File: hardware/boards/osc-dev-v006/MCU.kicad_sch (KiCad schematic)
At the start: 17 parts, among them J2 LINKE, J3 Qwiic, U2 CH32V006F8P6

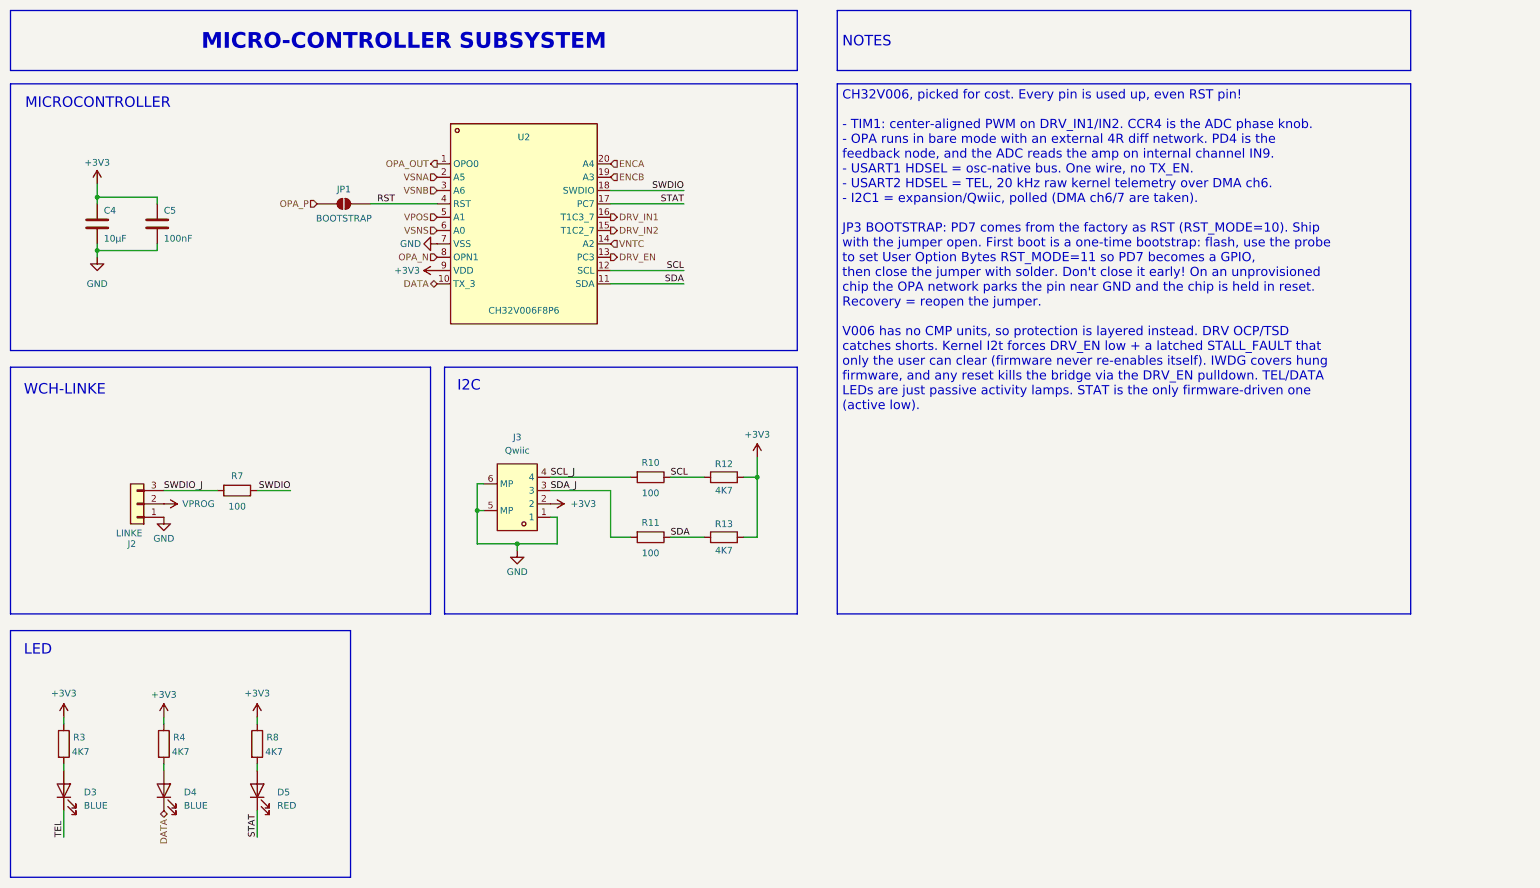
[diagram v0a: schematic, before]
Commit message: board: v006 rev-2a schematic refresh, family designators, terminal bias, tier-2 position input
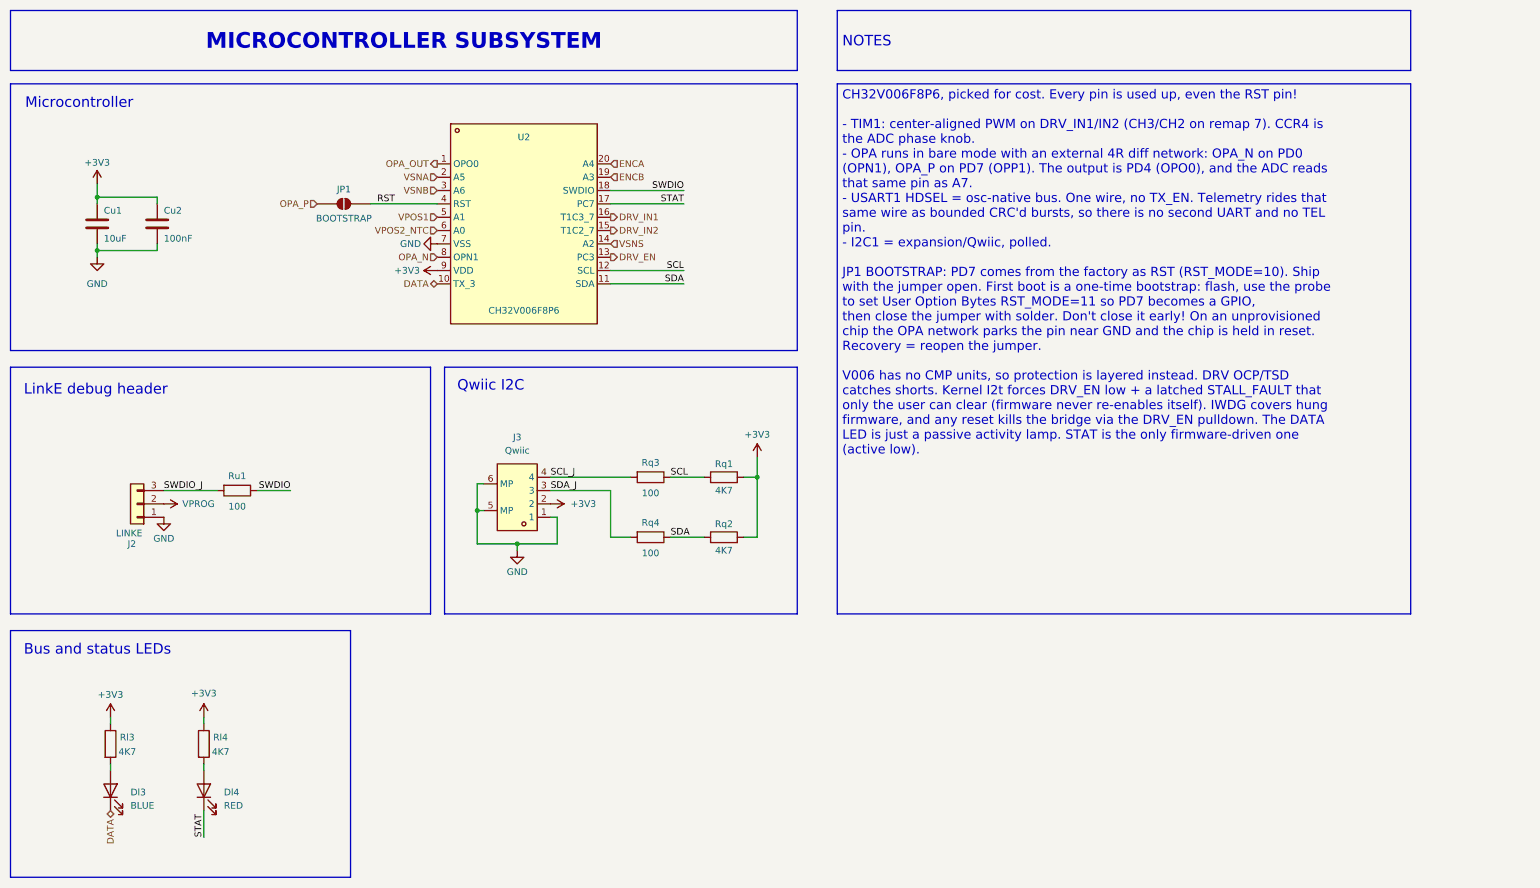
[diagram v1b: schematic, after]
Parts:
- removed D3: BLUE, LED_SMD:LED_0603_1608Metric_Pad1.05x0.95mm_HandSolder, symbol Device:LED
- removed R3: 4K7, Resistor_SMD:R_0603_1608Metric_Pad0.98x0.95mm_HandSolder, symbol Device:R
- Cu1: renamed from C4; value 10µF -> 10uF
- Dl3: renamed from D4; MFPN KT-0805B -> GL0603UB01
- Dl4: renamed from D5; LCSC C51933292 -> C497918; MFPN KT-0805R -> HL-PT-1608S52FC
- J2: footprint Connector_PinHeader_2.54mm:PinHeader_2x03_P2.54mm_Vertical -> Connector_PinHeader_2.54mm:PinHeader_1x03_P2.54mm_Vertical
- Rl3: renamed from R4; MFPN FRC0805F4701TS -> FRC0603F4701TS
- Rl4: renamed from R8; MFPN FRC0805F4701TS -> FRC0603F4701TS
- Rq1: renamed from R12; MFPN FRC0805F4701TS -> FRC0603F4701TS
- Rq2: renamed from R13; MFPN FRC0805F4701TS -> FRC0603F4701TS
- Rq3: renamed from R10; LCSC C2906981 -> C125923; MFPN FRC0805F1000TS -> (none)
- Rq4: renamed from R11; LCSC C2906981 -> C125923; MFPN FRC0805F1000TS -> (none)
- Ru1: renamed from R7; LCSC C2906981 -> C125923; MFPN FRC0805F1000TS -> (none)
- U2: JLC Type Extended -> (none)
- renumbered C5 to Cu2
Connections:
- net VNTC is gone; now on net VSNS: U2.14 (PC4)
- net VSNS: no longer U2.6 (PA2)
- net VPOS renamed VPOS1
- new net VPOS2_NTC: U2.6 (PA2)
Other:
- note added: "Bus and status LEDs"
- note added: "LinkE debug header"
- note added: "Microcontroller"
- note added: "Qwiic I2C"
- note removed: "I2C"
- note removed: "LED"
- note removed: "MICROCONTROLLER"
- note removed: "WCH-LINKE"
- moved on the sheet: Dl3, Dl4, Rl3, Rl4

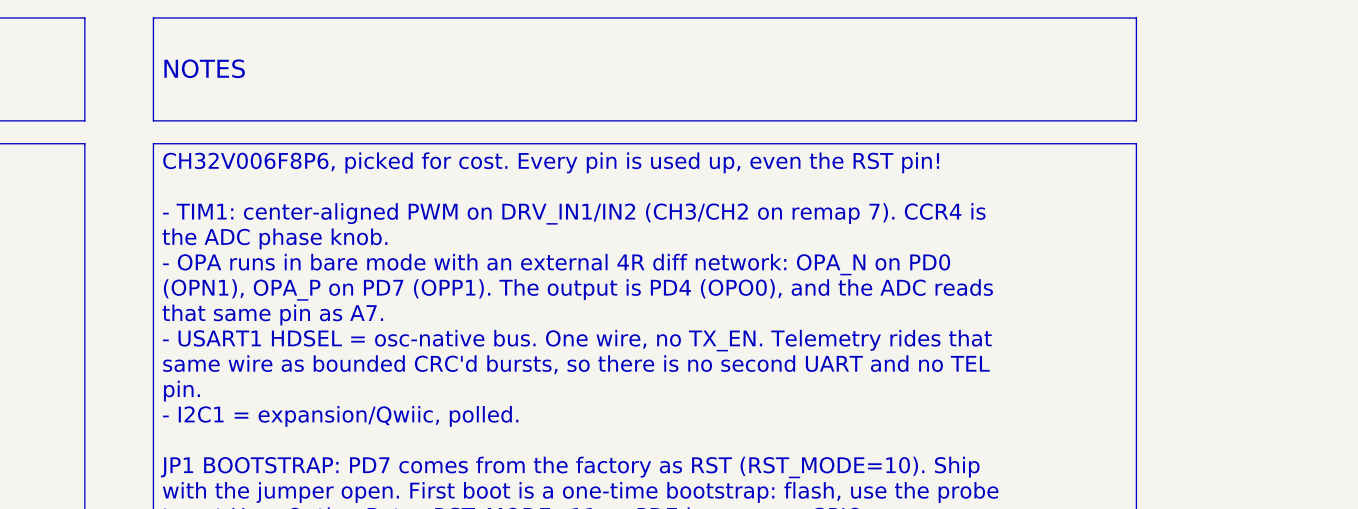
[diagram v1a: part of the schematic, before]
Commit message: board: v006 rev-2a audit fixes, rs2 deleted, rh2 jumper on the driver rail
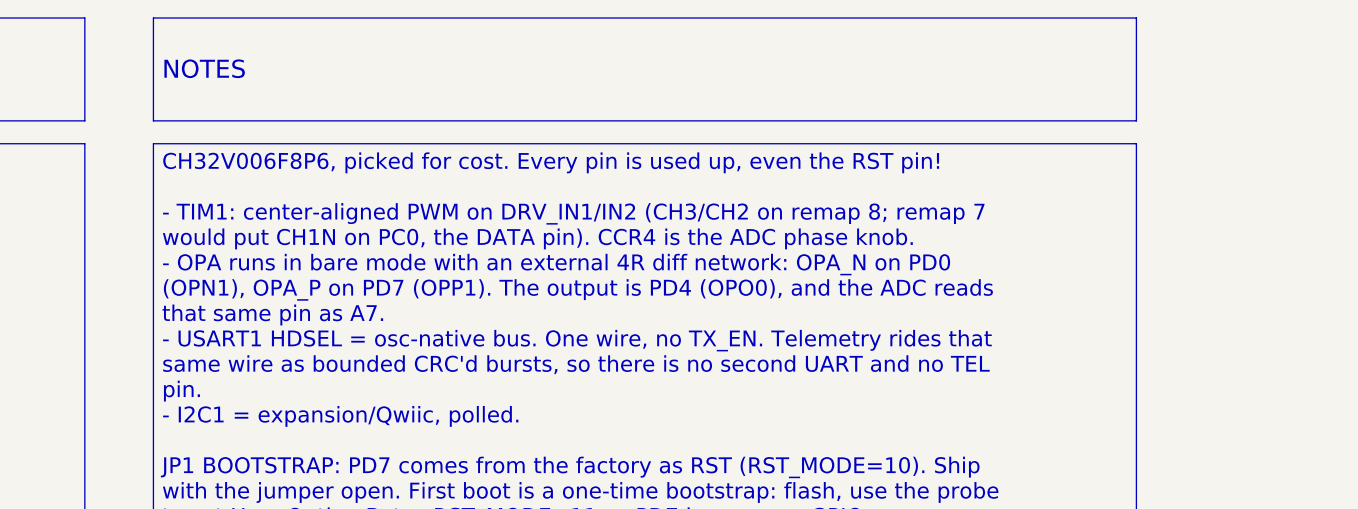
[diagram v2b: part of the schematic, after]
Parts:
- J2: LCSC C65114 -> C49257; MFPN 2.54-2*3P -> 2.54-1*3P
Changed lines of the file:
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@@
 		)
 	)
-	(text_box "CH32V006F8P6, picked for cost. Every pin is used up, even the RST pin!\n\n- TIM1: center-aligned PWM on DRV_IN1/IN2 (CH3/CH2 on remap 7). CCR4 is the ADC phase knob.\n- OPA runs in bare mode with an external 4R diff network: OPA_N on PD0 (OPN1), OPA_P on PD7 (OPP1). The output is PD4 (OPO0), and the ADC reads that same pin as A7.\n- USART1 HDSEL = osc-native bus. One wire, no TX_EN. Telemetry rides that same wire as bounded CRC'd bursts, so there is no second UART and no TEL pin.\n- I2C1 = expansion/Qwiic, polled.\n\nJP1 BOOTSTRAP: PD7 comes from the factory as RST (RST_MODE=10). Ship with the jumper open. First boot is a one-time bootstrap: flash, use the probe to set User Option Bytes RST_MODE=11 so PD7 becomes a GPIO,\nthen close the jumper with solder. Don't close it early! On an unprovisioned chip the OPA network parks the pin near GND and the chip is held in reset. Recovery = reopen the jumper.\n\nV006 has no CMP units, so protection is layered instead. DRV OCP/TSD catches shorts. Kernel I2t forces DRV_EN low + a latched STALL_FAULT that only the user can clear (firmware never re-enables itself). IWDG covers hung firmware, and any reset kills the bridge via the DRV_EN pulldown. The DATA LED is just a passive activity lamp. STAT is the only firmware-driven one (active low)."
+	(text_box "CH32V006F8P6, picked for cost. Every pin is used up, even the RST pin!\n\n- TIM1: center-aligned PWM on DRV_IN1/IN2 (CH3/CH2 on remap 8; remap 7 would put CH1N on PC0, the DATA pin). CCR4 is the ADC phase knob.\n- OPA runs in bare mode with an external 4R diff network: OPA_N on PD0 (OPN1), OPA_P on PD7 (OPP1). The output is PD4 (OPO0), and the ADC reads that same pin as A7.\n- USART1 HDSEL = osc-native bus. One wire, no TX_EN. Telemetry rides that same wire as bounded CRC'd bursts, so there is no second UART and no TEL pin.\n- I2C1 = expansion/Qwiic, polled.\n\nJP1 BOOTSTRAP: PD7 comes from the factory as RST (RST_MODE=10). Ship with the jumper open. First boot is a one-time bootstrap: flash, use the probe to set User Option Bytes RST_MODE=11 so PD7 becomes a GPIO,\nthen close the jumper with solder. Don't close it early! On an unprovisioned chip the OPA network parks the pin near GND and the chip is held in reset. Recovery = reopen the jumper.\n\nV006 has no CMP units, so protection is layered instead. DRV OCP/TSD catches shorts. Kernel I2t forces DRV_EN low + a latched STALL_FAULT that only the user can clear (firmware never re-enables itself). IWDG covers hung firmware, and any reset kills the bridge via the DRV_EN pulldown. The DATA LED is just a passive activity lamp. STAT is the only firmware-driven one (active low)."
 		(exclude_from_sim no)
 		(at 172.72 29.21 0)
@@
 			)
 		)
-		(property "Datasheet" "https://www.lcsc.com/product-detail/C65114.html"
+		(property "Datasheet" "https://www.lcsc.com/product-detail/C49257.html"
 			(at 39.37 109.22 0)
 			(hide yes)
@@
 			)
 		)
-		(property "LCSC" "C65114"
+		(property "LCSC" "C49257"
 			(at 39.37 118.11 0)
 			(hide yes)
@@
 			)
 		)
-		(property "MFPN" "2.54-2*3P"
+		(property "MFPN" "2.54-1*3P"
 			(at 39.37 118.11 0)
 			(hide yes)

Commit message: board: v006 rev-2a flex landing j11, rs1 hand-solder footprint
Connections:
- net GND: now also J2.2 (Pin_2); no longer J2.1 (Pin_1)
- net VPROG: now also J2.1 (Pin_1); no longer J2.2 (Pin_2)
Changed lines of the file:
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@@
+	)
+	(symbol
+		(lib_id "power:GND")
+		(at 44.45 109.22 90)
+		(unit 1)
+		(body_style 1)
+		(exclude_from_sim no)
+		(in_bom yes)
+		(on_board yes)
+		(in_pos_files yes)
+		(dnp no)
+		(property "Reference" "#PWR021"
+			(at 50.8 109.22 0)
+			(hide yes)
+			(show_name no)
+			(do_not_autoplace no)
+			(effects
+				(font
+					(size 1.27 1.27)
+				)
+			)
+		)
+		(property "Value" "GND"
+			(at 50.038 109.22 90)
+			(show_name no)
+			(do_not_autoplace no)
+			(effects
+				(font
+					(size 1.27 1.27)
+				)
+			)
+		)
+		(property "Footprint" ""
+			(at 44.45 109.22 0)
+			(hide yes)
+			(show_name no)
+			(do_not_autoplace no)
+			(effects
+				(font
+					(size 1.27 1.27)
+				)
+			)
+		)
+		(property "Datasheet" ""
+			(at 44.45 109.22 0)
+			(hide yes)
+			(show_name no)
+			(do_not_autoplace no)
+			(effects
+				(font
+					(size 1.27 1.27)
+				)
+			)
+		)
+		(property "Description" "Power symbol creates a global label with name \"GND\" , ground"
+			(at 44.45 109.22 0)
+			(hide yes)
+			(show_name no)
+			(do_not_autoplace no)
+			(effects
+				(font
+					(size 1.27 1.27)
+				)
+			)
+		)
+		(pin "1"
+		)
+		(instances
+			(project "osc-dev-v006"
+				(path "/6062e7d2-0c72-467e-b49c-6387ba053e09/77d3819f-1672-490a-859c-8df54ad0ab77"
+					(reference "#PWR021")
+					(unit 1)
+				)
+			)
+		)
 	)
 	(symbol
@@
 	)
 	(symbol
-		(lib_id "power:VBUS")
-		(at 44.45 109.22 270)
-		(unit 1)
-		(body_style 1)
-		(exclude_from_sim no)
-		(in_bom yes)
-		(on_board yes)
-		(in_pos_files yes)
-		(dnp no)
-		(property "Reference" "#PWR020"
-			(at 40.64 109.22 0)
-			(hide yes)
-			(show_name no)
-			(do_not_autoplace no)
-			(effects
-				(font
-					(size 1.27 1.27)
-				)
-			)
-		)
-		(property "Value" "VPROG"
-			(at 51.054 109.22 90)
-			(show_name no)
-			(do_not_autoplace no)
-			(effects
-				(font
-					(size 1.27 1.27)
-				)
-			)
-		)
-		(property "Footprint" ""
-			(at 44.45 109.22 0)
-			(hide yes)
-			(show_name no)
-			(do_not_autoplace no)
-			(effects
-				(font
-					(size 1.27 1.27)
-				)
-			)
-		)
-		(property "Datasheet" ""
-			(at 44.45 109.22 0)
-			(hide yes)
-			(show_name no)
-			(do_not_autoplace no)
-			(effects
-				(font
-					(size 1.27 1.27)
-				)
-			)
-		)
-		(property "Description" "Power symbol creates a global label with name \"VBUS\""
-			(at 44.45 109.22 0)
-			(hide yes)
-			(show_name no)
-			(do_not_autoplace no)
-			(effects
-				(font
-					(size 1.27 1.27)
-				)
-			)
-		)
-		(pin "1"
-		)
-		(instances
-			(project "osc-dev-v006"
-				(path "/6062e7d2-0c72-467e-b49c-6387ba053e09/77d3819f-1672-490a-859c-8df54ad0ab77"
-					(reference "#PWR020")
-					(unit 1)
-				)
-			)
-		)
-	)
-	(symbol
 		(lib_id "Connector_Generic:Conn_01x03")
 		(at 39.37 109.22 180)
@@
 	)
 	(symbol
-		(lib_id "power:GND")
-		(at 44.45 111.76 0)
+		(lib_id "power:VBUS")
+		(at 44.45 111.76 270)
 		(unit 1)
 		(body_style 1)
@@
 		(in_pos_files yes)
 		(dnp no)
-		(property "Reference" "#PWR021"
-			(at 44.45 118.11 0)
-			(hide yes)
-			(show_name no)
-			(do_not_autoplace no)
-			(effects
-				(font
-					(size 1.27 1.27)
-				)
-			)
-		)
-		(property "Value" "GND"
-			(at 44.45 115.824 0)
+		(property "Reference" "#PWR020"
+			(at 40.64 111.76 0)
+			(hide yes)
+			(show_name no)
+			(do_not_autoplace no)
+			(effects
+				(font
+					(size 1.27 1.27)
+				)
+			)
+		)
+		(property "Value" "VPROG"
+			(at 51.054 111.76 90)
 			(show_name no)
 			(do_not_autoplace no)
@@
 			)
 		)
-		(property "Description" "Power symbol creates a global label with name \"GND\" , ground"
+		(property "Description" "Power symbol creates a global label with name \"VBUS\""
 			(at 44.45 111.76 0)
 			(hide yes)
@@
 			(project "osc-dev-v006"
 				(path "/6062e7d2-0c72-467e-b49c-6387ba053e09/77d3819f-1672-490a-859c-8df54ad0ab77"
-					(reference "#PWR021")
-					(unit 1)
-				)
+					(reference "#PWR020")
+					(unit 1)
+				)
